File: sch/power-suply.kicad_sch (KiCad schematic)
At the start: 37 parts, among them J9 12V_in, Q2 DMT6007LFG-7, U6 LM74700QDBVTQ1, U7 LMR51450SDRRR, U8 LMR51450SDRRR

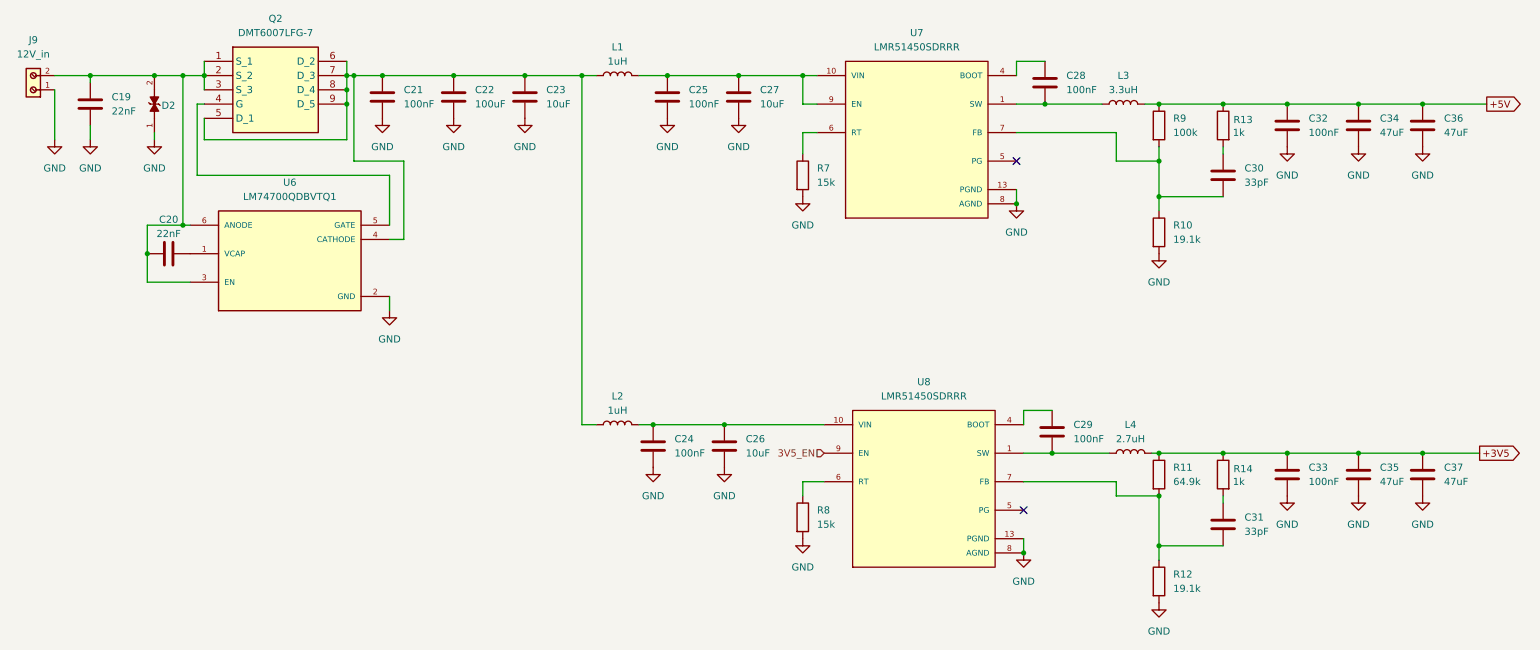
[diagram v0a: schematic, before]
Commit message: lagt inn footprint på alt, obs feil footprint i pwr-supply
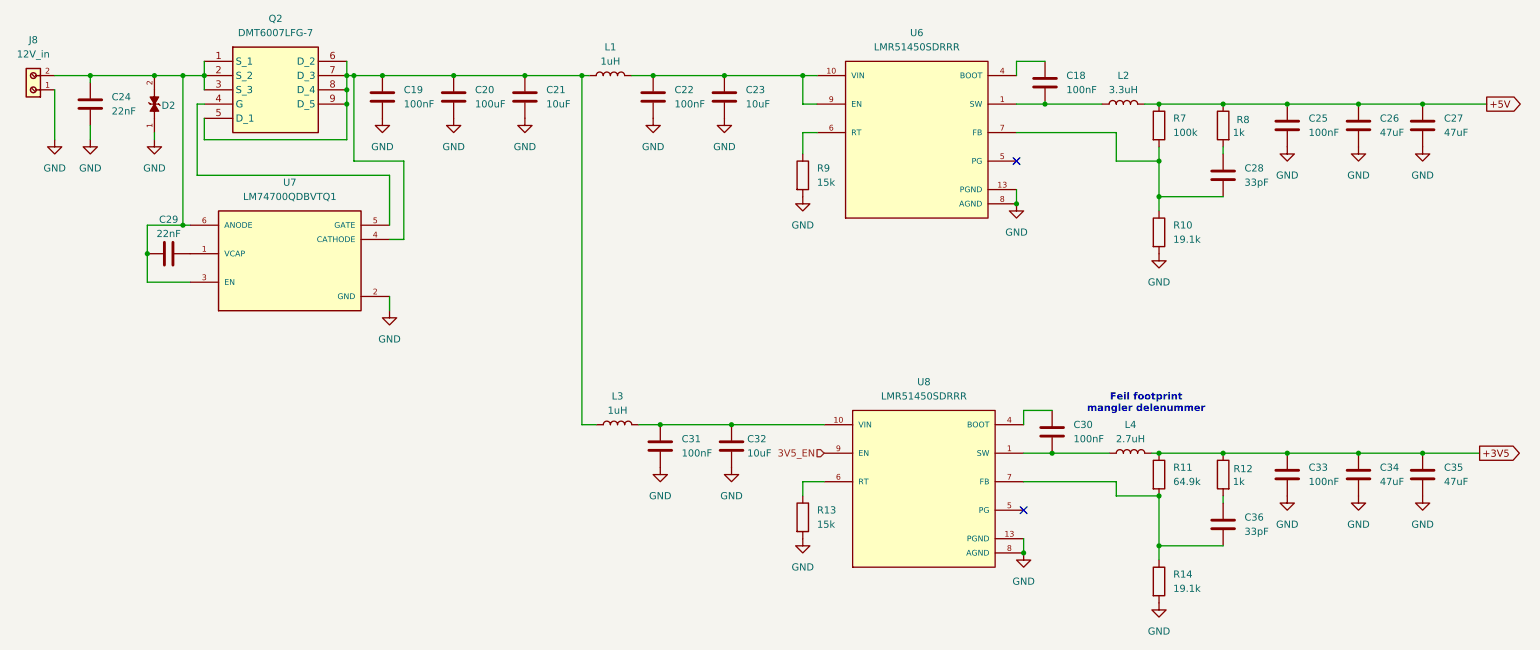
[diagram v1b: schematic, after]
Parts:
- removed C24, C29: 100nF, symbol Device:C
- removed C26: 10uF, symbol Device:C
- removed C36, C37: 47uF, symbol Device:C
- removed L2: 1uH, symbol Device:L
- added C23, C32: 10uF, Capacitor_SMD:C_1210_3225Metric, symbol Device:C
- added C28: 33pF, Capacitor_SMD:C_0603_1608Metric, symbol Device:C
- added C31: 100nF, Capacitor_SMD:C_0603_1608Metric, symbol Device:C
- added C34: 47uF, Capacitor_SMD:C_1210_3225Metric, symbol Device:C
- added L3: 1uH, LQM2HPN1R0MJHL:INDC2520X120N, symbol Device:L
- C20: renamed from C22; footprint (none) -> Capacitor_SMD:C_1210_3225Metric; MPN (none) -> C1210C107M4PACTU
- C21: renamed from C23; footprint (none) -> Capacitor_SMD:C_1210_3225Metric; MPN (none) -> C1210C106M4PACTU
- C26: renamed from C34; footprint (none) -> Capacitor_SMD:C_1210_3225Metric; MPN (none) -> C1210C476M4PACTU
- C27: value 10uF -> 47uF; footprint (none) -> Capacitor_SMD:C_1210_3225Metric; MPN (none) -> C1210C476M4PACTU
- C30: value 33pF -> 100nF; footprint (none) -> Capacitor_SMD:C_0603_1608Metric; MPN (none) -> C0603C104K3RACTU
- C33: footprint (none) -> Capacitor_SMD:C_0603_1608Metric; MPN (none) -> C0603C104K3RACTU
- C35: footprint (none) -> Capacitor_SMD:C_1210_3225Metric; MPN (none) -> C1210C476M4PACTU
- C36: renamed from C31; footprint (none) -> Capacitor_SMD:C_0603_1608Metric; MPN (none) -> C0603C330K5RACTU
- L1: footprint (none) -> LQM2HPN1R0MJHL:INDC2520X120N; MPN (none) -> LQM2HPN1R0MJHL
- L2: renamed from L3; footprint (none) -> WE-LHMI_7050:WE-LHMI_7050; MPN (none) -> 74437349033
- L4: footprint (none) -> Inductor_SMD_Wurth:L_Wurth_WE-LQSH-2512; OBS (none) -> Feil footprint per 18.03
- renumbered C28 to C18, C21 to C19, C25 to C22, C19 to C24, C32 to C25, C20 to C29, J9 to J8, R14 to R12, R8 to R13, R12 to R14, R9 to R7, R13 to R8, R7 to R9, U7 to U6, U6 to U7
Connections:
- net +3V5: now also C34.1
- net +5V: now also C27.1
- net GND: now also C23.2, C31.2, C32.2, C34.2
- net at C22.1, L1.2, U6.10 (VIN)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: now also C23.1; no longer C27.1
- net at R10.1, R7.2, U6.7 (FB): now also C28.2; no longer C30.2
- net at U8.10 (VIN), U8.11 (VIN), U8.12 (VIN): now also C31.1, C32.1, L3.2
- net at C19.1, C20.1, C21.1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: now also L3.1
- net at R8.2: now also C28.1; no longer C30.1
- net at L4.1, U8.1 (SW), U8.2 (SW)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: now also C30.2
- net at U8.4 (BOOT): now also C30.1
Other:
- note added: "Feil footprint mangler delenummer"
- moved on the sheet: C22, L1

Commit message: Fjernet gammelt og la til nye komponenter, merging ferdig
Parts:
- removed C20: 100uF, Capacitor_SMD:C_1210_3225Metric, symbol Device:C
- removed C21: 10uF, Capacitor_SMD:C_1210_3225Metric, symbol Device:C
- added C?: 100uF, CAPPRD350W60D825H1350, symbol 50ZLH100MEFC8X11_5:50ZLH100MEFC8X11.5
- added C? (x2): 10uF, Capacitor_SMD:C_1210_3225Metric, symbol Device:C
- L?: renamed from L4; footprint Inductor_SMD_Wurth:L_Wurth_WE-LQSH-2512 -> SLF12575T-2R7N7R0-H:IND_SLF12575T-2R7N7R0-H; MPN (none) -> SLF12575T-2R7N7R0-H
- renumbered C28 to C?, C35 to C?, C29 to C?, C31 to C?, C19 to C?, C33 to C?, C18 to C?, C24 to C?, C23 to C?, C22 to C?, C25 to C?, C26 to C?, C36 to C?, C32 to C?, C30 to C?, C27 to C?, C34 to C?, D2 to D?, J8 to J?, L1 to L?, L3 to L?, L2 to L?, Q2 to Q?, R13 to R?, R10 to R?, R9 to R?, R14 to R?, R8 to R?, R12 to R?, R11 to R?, R7 to R?, U6 to U?, U7 to U?, U8 to U?
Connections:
- net 3V5_EN is gone; now on an unnamed net: U?.9 (EN)
- net GND: now also C?.2, C?.2, C?.2 (-)
- net at C?.1, C?.1, L?.2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: now also C?.1, L?.1, L?.1, Q?.5 (D_1), Q?.6 (D_2), Q?.7 (D_3), Q?.8 (D_4), Q?.9 (D_5), U?.4 (CATHODE), C?.1, C?.1 (+)
- net +12V: now reaches C?.1, C?.1, D?.2, J?.2, Q?.1 (S_1), Q?.2 (S_2), Q?.3 (S_3), U?.3 (EN), U?.6 (ANODE)
- net at C?.1, C?.1, L?.2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: now also C?.1
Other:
- note removed: "Feil footprint mangler delenummer"
- moved on the sheet: L?

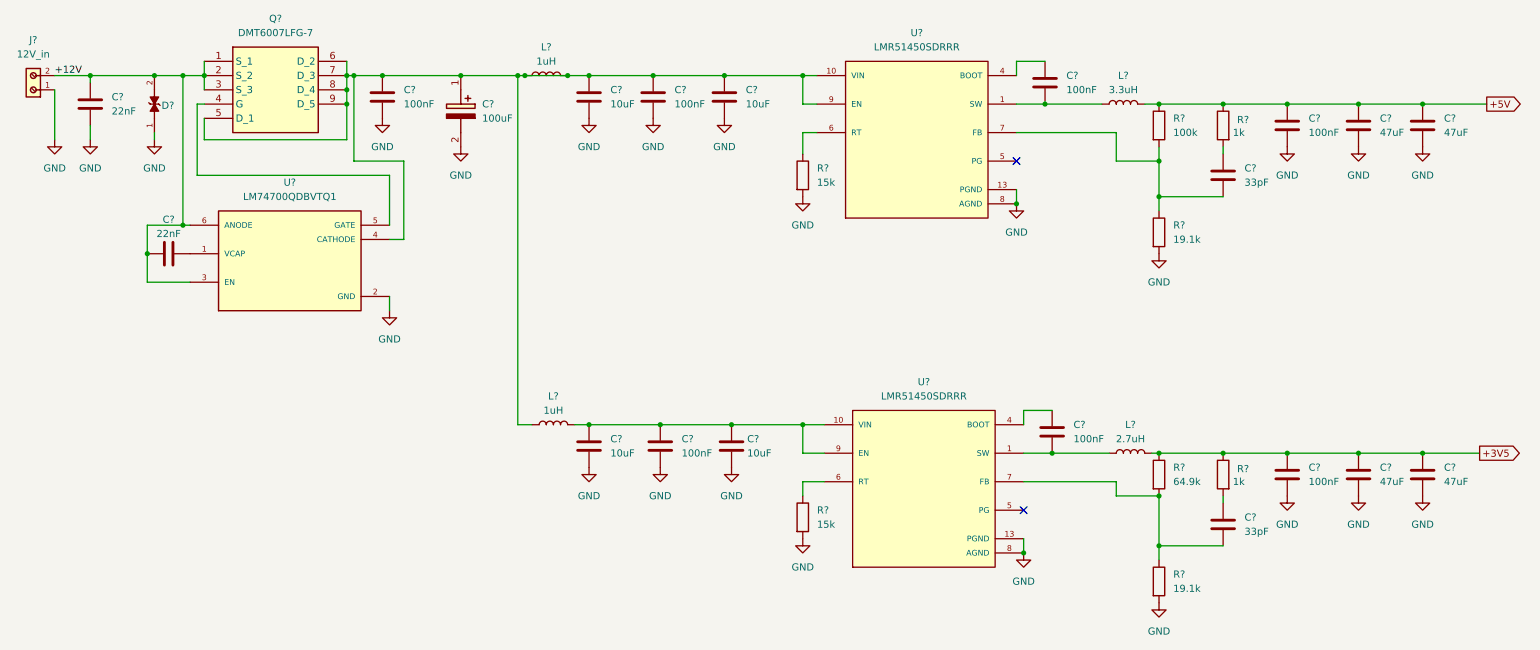
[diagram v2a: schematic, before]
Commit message: Ferdig pcb-layout modem og simkort, ikke kobla til CM enda
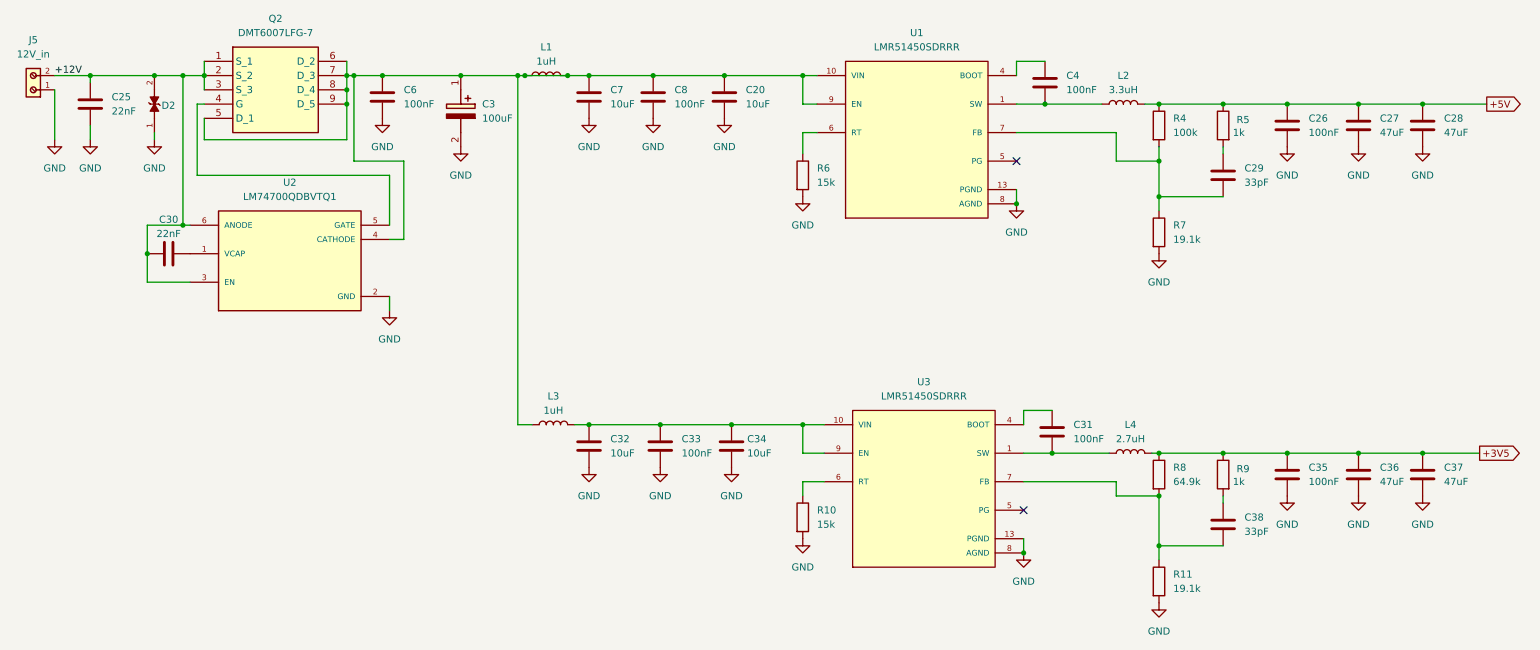
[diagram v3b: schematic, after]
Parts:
- gave numbers to parts that had none: 38

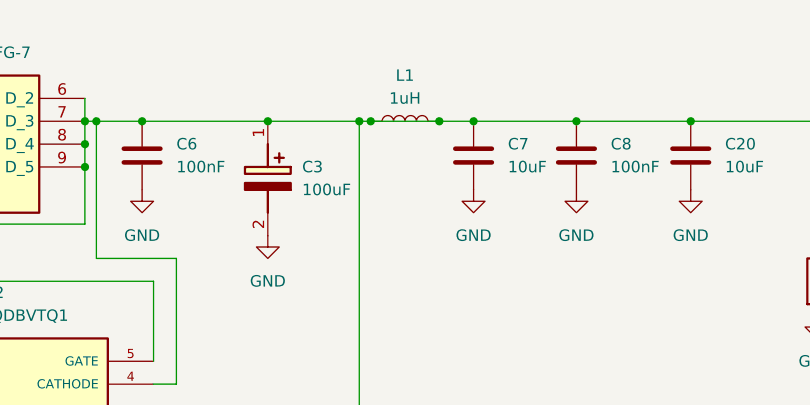
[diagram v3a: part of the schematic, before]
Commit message: powersupply routingalmost complete, missing som ground vias and connection to modem
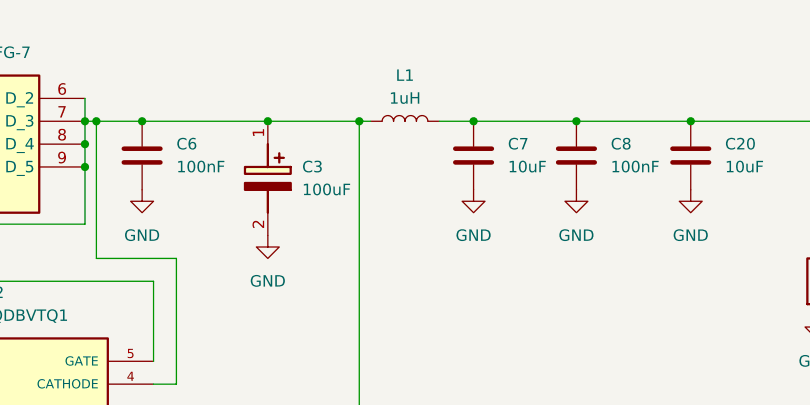
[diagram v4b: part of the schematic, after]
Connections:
- net at C3.1 (+), C6.1, L1.1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: no longer C20.1, C7.1, C8.1, L1.2, U1.10 (VIN), U1.11 (VIN), U1.12 (VIN), U1.9 (EN)
- new net: C20.1, C7.1, C8.1, L1.2, U1.10 (VIN), U1.11 (VIN), U1.12 (VIN), U1.9 (EN)
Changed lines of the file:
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@@
-	)
-	(junction
-		(at 105.41 26.67)
-		(diameter 0)
-		(color 0 0 0 0)
 	)
 	(junction
@@
 	(junction
 		(at 104.14 26.67)
-		(diameter 0)
-		(color 0 0 0 0)
-	)
-	(junction
-		(at 113.03 26.67)
 		(diameter 0)
 		(color 0 0 0 0)
@@
 		)
 		(stroke
-			(width 0)
-			(type default)
-		)
-	)
-	(wire
-		(pts
-			(xy 105.41 26.67) (xy 113.03 26.67)
-		)
-		(stroke

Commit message: Homestretch
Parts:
- R8: footprint Resistor_SMD:R_0201_0603Metric -> Resistor_SMD:R_0603_1608Metric
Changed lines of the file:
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@@
 		)
 		(property "Value" "100nF"
-			(at 245.11 99.0599 0)
+			(at 245.364 99.314 0)
 			(effects
 				(font
@@
 			)
 		)
-		(property "Footprint" "Resistor_SMD:R_0201_0603Metric"
+		(property "Footprint" "Resistor_SMD:R_0603_1608Metric"
 			(at 216.662 97.79 90)
 			(effects
